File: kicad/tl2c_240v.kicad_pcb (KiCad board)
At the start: 2 copper layers, 63.5 x 66 mm, 24 parts, among them P106 240VAC, P107 LED_DRIVER, P108 LED_OUT, Q401 IRLML2502, Q402 IRLML2502, Q403 IRLML2502

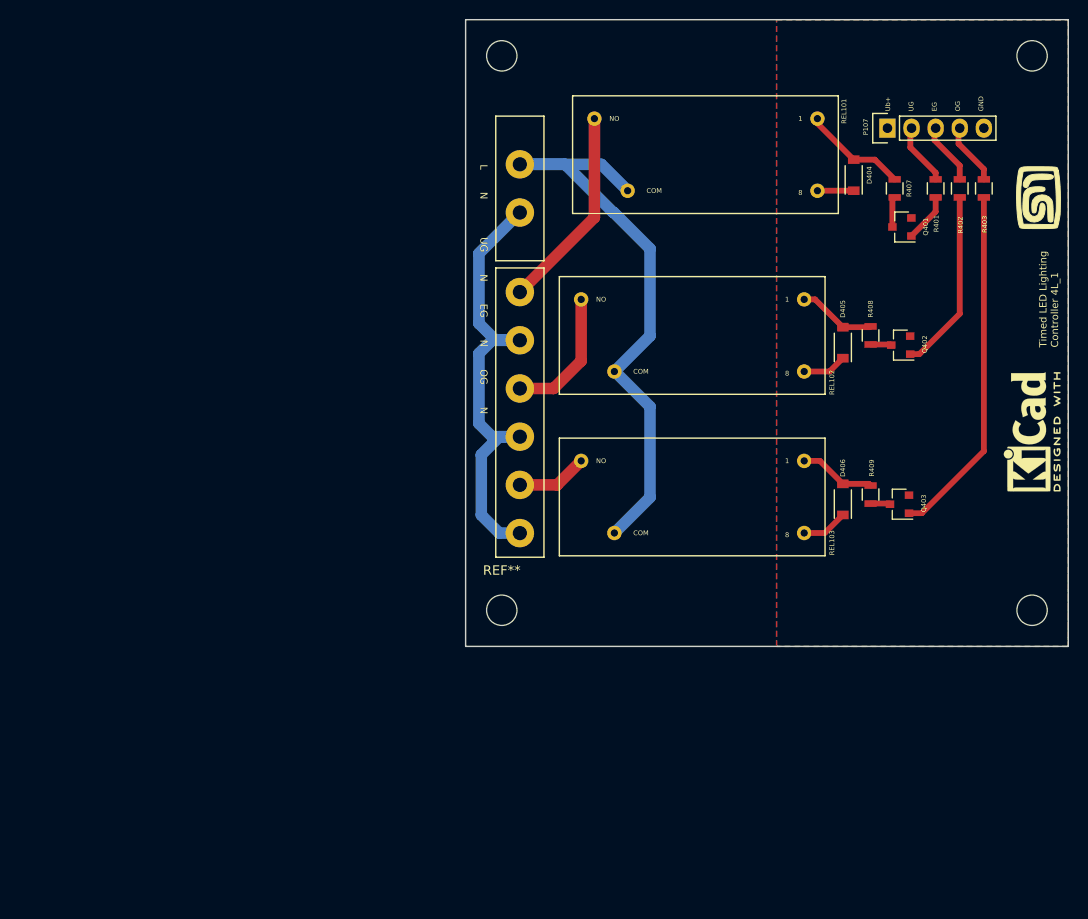
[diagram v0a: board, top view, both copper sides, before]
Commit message: Created the Gerbers and submitted the order for boards and stensils
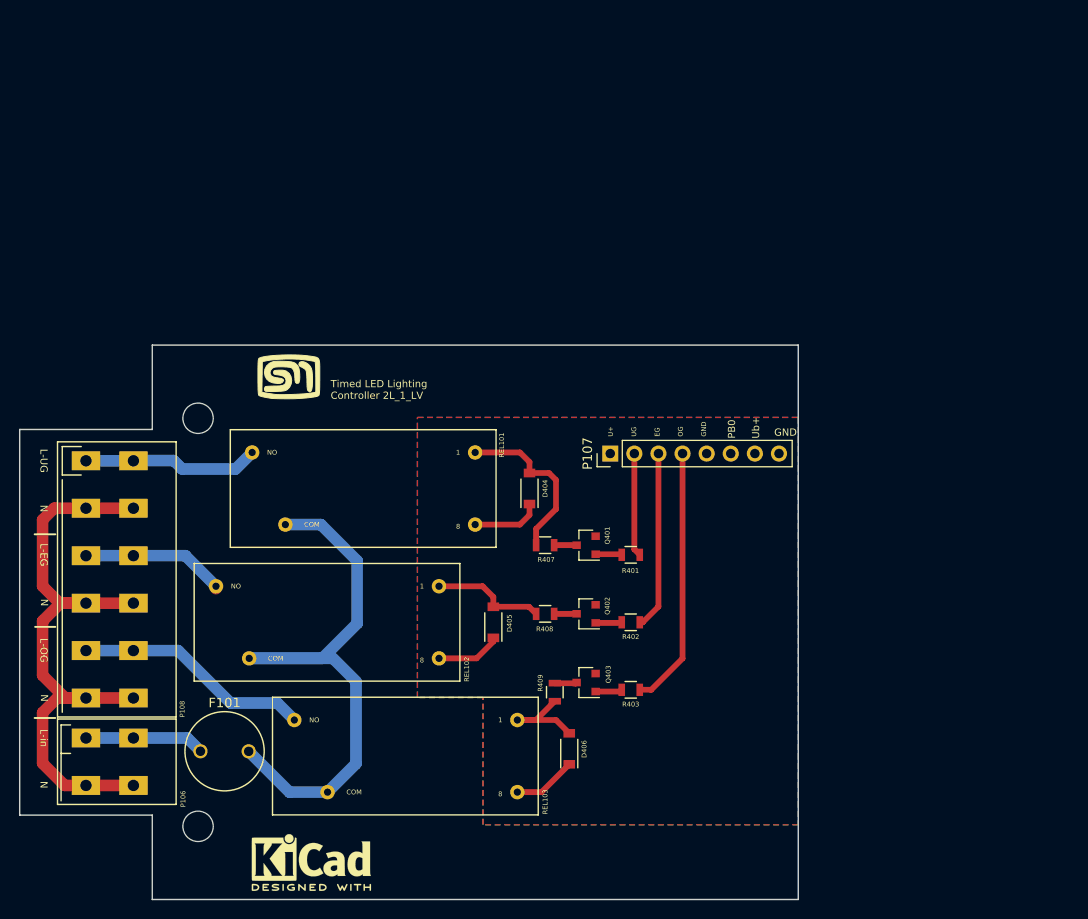
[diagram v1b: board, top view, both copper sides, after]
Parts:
- removed the REF** at (141.0, 80.0)
- removed the REF** at (141.0, 21.6)
- removed the REF** at (85.1, 80.0)
- added F101: 500mA, tl2c-footprint:Fuse_TE5_Littlefuse-ESKA_887_O14, F.Cu at (55.9, 94.9)
- added REF**: MountingHole_3.2mm_M3, Mounting_Holes:MountingHole_3.2mm_M3, F.Cu at (53.1, 102.8)
- P106: footprint tl2c-footprint:Pin_Header_1_x_2_5mmPitch -> tl2c-footprint:TERMINAL_BLOCK_2_5MM_5MM
- P107: footprint Pin_Headers:Pin_Header_Straight_1x05 -> Pin_Headers:Pin_Header_Straight_1x08_Pitch2.54mm
- P108: footprint tl2c-footprint:Pin_Header_1_x_6_54mmPitch -> tl2c-footprint:TERMINAL_BLOCK_6_5MM_5MM
- moved REF*** 88.5 mm to (65.0, 106.6), turned to 0 degrees
- moved G*** 81.2 mm to (62.6, 55.4), turned to 0 degrees
- moved P106 73.8 mm to (41.3, 93.5), turned to 0 degrees
- moved R403 64.6 mm to (98.7, 88.4), turned to 0 degrees
- moved R402 57.4 mm to (98.7, 81.3), turned to 0 degrees
- moved R407 52.6 mm to (89.7, 73.2), turned to 0 degrees
- moved REL101 50.4 mm to (70.5, 67.2)
- moved R401 50.2 mm to (98.7, 74.2), turned to 0 degrees
- moved REF** 49.8 mm to (53.1, 59.8)
- moved REL102 48.9 mm to (66.7, 81.3)
- moved D404 47.5 mm to (88.0, 67.2)
- moved Q401 47.2 mm to (94.0, 73.2)
- moved D405 47.2 mm to (84.2, 81.3)
- moved P108 46.0 mm to (41.3, 64.3), turned to 0 degrees
- moved R408 45.1 mm to (89.7, 80.4), turned to 0 degrees
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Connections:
- P107 pad 5: GNDA -> Net-(P107-Pad5)
- REL101 pad 6: /Lin -> Net-(F101-Pad2)
- REL102 pad 6: /Lin -> Net-(F101-Pad2)
- REL103 pad 6: /Lin -> Net-(F101-Pad2)
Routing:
- net Net-(F101-Pad2): track 0.00 -> 64.0 mm
- net /Lin: track 64.5 -> 12.6 mm
- net Net-(Q403-Pad1): track 37.3 -> 2.83 mm
- net /LED Driver/Relay_OG: track 6.38 -> 27.5 mm
- net /Neutral: track 51.7 -> 70.1 mm
- net /LineOG: track 7.51 -> 25.0 mm
- net Net-(Q402-Pad1): track 19.2 -> 2.77 mm
- net /LED Driver/Relay_EG: track 6.38 -> 18.8 mm
- net /LED Driver/LED_DRIVER_U+: track 13.7 -> 20.7 mm
- net Net-(D404-Pad2): track 11.1 -> 18.0 mm
- net /LED Driver/Relay_UG: track 6.38 -> 10.9 mm
- net Net-(D405-Pad2): track 8.24 -> 12.0 mm
- net /LineUG: track 21.5 -> 18.6 mm
- net Net-(D406-Pad2): track 8.07 -> 10.8 mm
- net Net-(Q401-Pad1): track 5.12 -> 2.78 mm
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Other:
- board size 63.5 x 66 mm -> 82 x 58.4 mm
- rule pad_to_mask_clearance: 0.2 -> 0
- board text added: "GND"
- board text added: "L-EG"
- board text added: "L-OG"
- board text added: "L-UG"
- board text added: "L-in"
- board text added: "N"
- board text added: "PB0"
- board text added: "Timed LED Lighting Controller 2L_1_LV"
- board text added: "U+ UG EG OG GND"
- board text added: "Ub+"
- board text removed: "L N UG N EG N OG N"
- board text removed: "Timed LED Lighting Controller 4L_1"
- board text removed: "Ub+ UG EG OG GND"

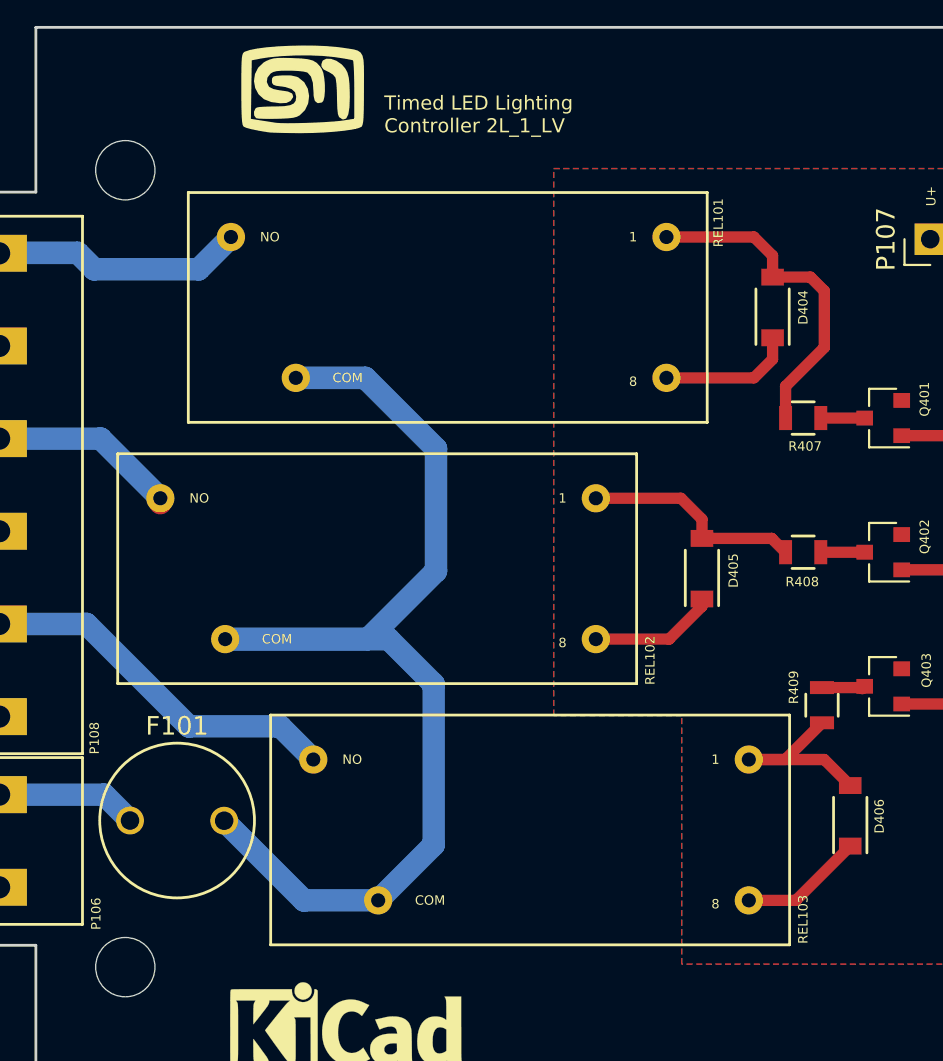
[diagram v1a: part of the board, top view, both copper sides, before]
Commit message: Updated the footprint for the relay - larger holes
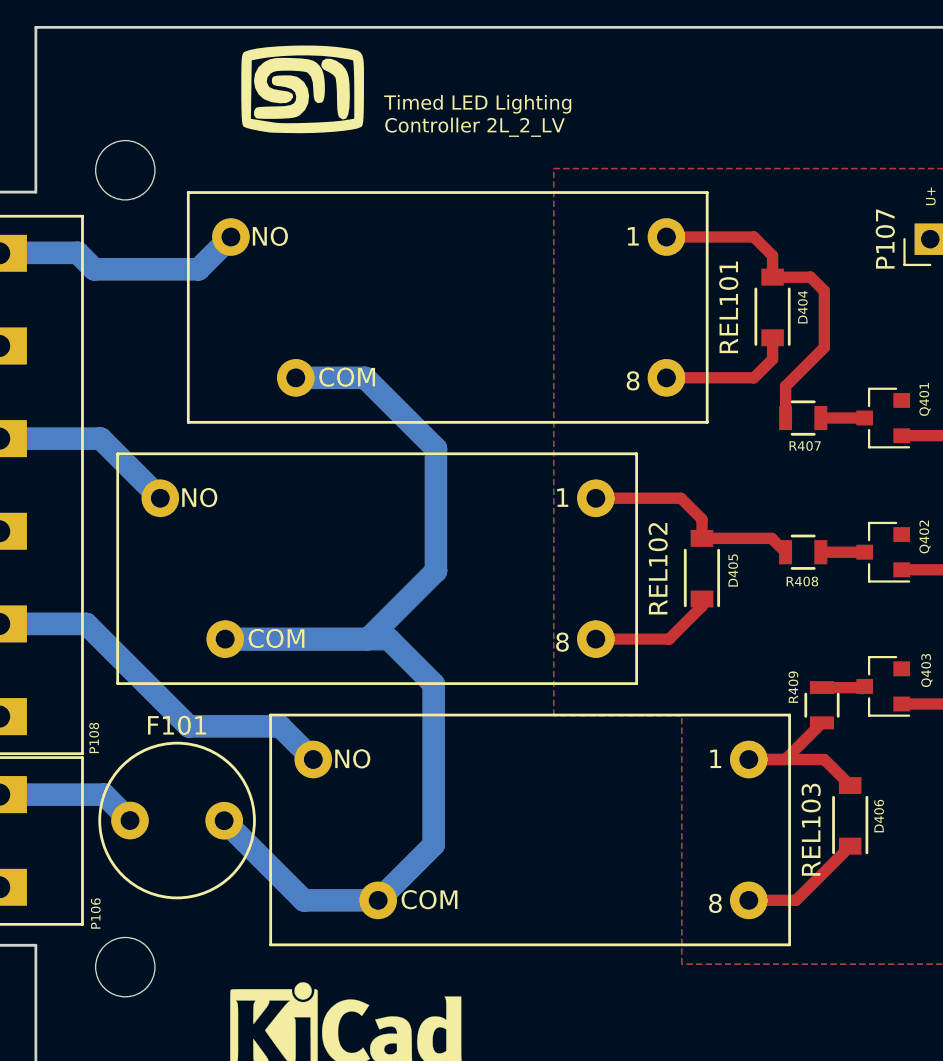
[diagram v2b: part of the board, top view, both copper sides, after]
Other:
- board text added: "Timed LED Lighting Controller 2L_2_LV"
- board text removed: "Timed LED Lighting Controller 2L_1_LV"
